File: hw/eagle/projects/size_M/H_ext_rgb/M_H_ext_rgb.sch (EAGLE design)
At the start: 6 parts

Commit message: pcb M.1 -not finished
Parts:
- removed U$2: RGB_WW-FCE50TC-Q1, !stavebnice03:RGB_WW-FCE50TC-Q1
- added H.D1: RGB_WW-FCE50TC-Q1, hugo:RGB_WW-FCE50TC-Q1
- H.R1, H.R2, H.R3: value 330 -> 82
- renumbered JP2 to H.J2, JP3 to H.J3, R1 to H.R1, R2 to H.R2, R3 to H.R3
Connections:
- net GND: now also H.D1.4, H.D1.5, H.D1.6, H.J3.4; no longer H.J3.3, U$2.4, U$2.5, U$2.6
- net N$1: now also H.D1.1; no longer U$2.1
- net N$2: now also H.D1.3; no longer U$2.3
- net N$3: now also H.D1.2; no longer U$2.2
- net VDD: now also H.J3.3; no longer H.J3.4
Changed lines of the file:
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@@
 </classes>
 <parts>
-<part name="JP2" library="pinhead2" deviceset="PINHD-1X6" device="" package3d_urn="urn:adsk.eagle:package:22472/2"/>
-<part name="U$2" library="!stavebnice03" deviceset="RGB_WW-FCE50TC-Q1" device=""/>
-<part name="R1" library="resistor" deviceset="R-EU_" device="R0603" value="330"/>
-<part name="R2" library="resistor" deviceset="R-EU_" device="R0603" value="330"/>
-<part name="R3" library="resistor" deviceset="R-EU_" device="R0603" value="330"/>
-<part name="JP3" library="pinhead2" deviceset="PINHD-1X5" device="" package3d_urn="urn:adsk.eagle:package:22469/2"/>
+<part name="H.J2" library="pinhead2" deviceset="PINHD-1X6" device="" package3d_urn="urn:adsk.eagle:package:22472/2"/>
+<part name="H.D1" library="hugo" deviceset="RGB_WW-FCE50TC-Q1" device=""/>
+<part name="H.R1" library="resistor" deviceset="R-EU_" device="R0603" value="82"/>
+<part name="H.R2" library="resistor" deviceset="R-EU_" device="R0603" value="82"/>
+<part name="H.R3" library="resistor" deviceset="R-EU_" device="R0603" value="82"/>
+<part name="H.J3" library="pinhead2" deviceset="PINHD-1X5" device="" package3d_urn="urn:adsk.eagle:package:22469/2"/>
 </parts>
 <sheets>
@@
 </plain>
 <instances>
-<instance part="JP2" gate="A" x="-15.24" y="48.26" smashed="yes" rot="R180">
+<instance part="H.J2" gate="A" x="-15.24" y="48.26" smashed="yes" rot="R180">
 <attribute name="NAME" x="-8.89" y="37.465" size="1.778" layer="95" rot="R180"/>
 <attribute name="VALUE" x="-8.89" y="58.42" size="1.778" layer="96" rot="R180"/>
 </instance>
-<instance part="U$2" gate="G$1" x="17.78" y="60.96" smashed="yes" rot="R180">
+<instance part="H.D1" gate="G$1" x="17.78" y="60.96" smashed="yes" rot="R180">
 <attribute name="NAME" x="27.94" y="66.04" size="1.27" layer="94" rot="R270"/>
 </instance>
-<instance part="R1" gate="G$1" x="5.08" y="86.36" smashed="yes" rot="MR180">
+<instance part="H.R1" gate="G$1" x="5.08" y="86.36" smashed="yes" rot="MR180">
 <attribute name="NAME" x="1.27" y="84.8614" size="1.778" layer="95" rot="MR180"/>
 <attribute name="VALUE" x="1.27" y="89.662" size="1.778" layer="96" rot="MR180"/>
 </instance>
-<instance part="R2" gate="G$1" x="5.08" y="78.74" smashed="yes" rot="MR180">
+<instance part="H.R2" gate="G$1" x="5.08" y="78.74" smashed="yes" rot="MR180">
 <attribute name="NAME" x="1.27" y="77.2414" size="1.778" layer="95" rot="MR180"/>
 <attribute name="VALUE" x="1.27" y="82.042" size="1.778" layer="96" rot="MR180"/>
 </instance>
-<instance part="R3" gate="G$1" x="5.08" y="71.12" smashed="yes" rot="MR180">
+<instance part="H.R3" gate="G$1" x="5.08" y="71.12" smashed="yes" rot="MR180">
 <attribute name="NAME" x="1.27" y="69.6214" size="1.778" layer="95" rot="MR180"/>
 <attribute name="VALUE" x="1.27" y="74.422" size="1.778" layer="96" rot="MR180"/>
 </instance>
-<instance part="JP3" gate="A" x="38.1" y="45.72" smashed="yes">
+<instance part="H.J3" gate="A" x="38.1" y="45.72" smashed="yes">
 <attribute name="NAME" x="31.75" y="53.975" size="1.778" layer="95"/>
 <attribute name="VALUE" x="31.75" y="35.56" size="1.778" layer="96"/>
@@
 <segment>
 <wire x1="17.78" y1="78.74" x2="10.16" y2="78.74" width="0.1524" layer="91"/>
-<pinref part="R2" gate="G$1" pin="2"/>
-<pinref part="U$2" gate="G$1" pin="2"/>
+<pinref part="H.R2" gate="G$1" pin="2"/>
+<pinref part="H.D1" gate="G$1" pin="2"/>
 <wire x1="17.78" y1="78.74" x2="17.78" y2="71.12" width="0.1524" layer="91"/>
 </segment>
@@
 <wire x1="12.7" y1="45.72" x2="22.86" y2="45.72" width="0.1524" layer="91"/>
 <junction x="12.7" y="45.72"/>
-<pinref part="U$2" gate="G$1" pin="6"/>
+<pinref part="H.D1" gate="G$1" pin="6"/>
 <wire x1="12.7" y1="48.26" x2="12.7" y2="45.72" width="0.1524" layer="91"/>
 <junction x="12.7" y="45.72"/>
-<pinref part="U$2" gate="G$1" pin="5"/>
+<pinref part="H.D1" gate="G$1" pin="5"/>
 <wire x1="17.78" y1="48.26" x2="17.78" y2="45.72" width="0.1524" layer="91"/>
 <junction x="17.78" y="45.72"/>
-<pinref part="U$2" gate="G$1" pin="4"/>
+<pinref part="H.D1" gate="G$1" pin="4"/>
 <wire x1="22.86" y1="48.26" x2="22.86" y2="45.72" width="0.1524" layer="91"/>
 <junction x="22.86" y="45.72"/>
-<wire x1="35.56" y1="45.72" x2="22.86" y2="45.72" width="0.1524" layer="91"/>
 <junction x="22.86" y="45.72"/>
-<pinref part="JP3" gate="A" pin="3"/>
-<pinref part="JP2" gate="A" pin="6"/>
+<pinref part="H.J2" gate="A" pin="6"/>
 <wire x1="-12.7" y1="53.34" x2="7.62" y2="53.34" width="0.1524" layer="91"/>
 <wire x1="7.62" y1="53.34" x2="7.62" y2="45.72" width="0.1524" layer="91"/>
 <wire x1="7.62" y1="45.72" x2="12.7" y2="45.72" width="0.1524" layer="91"/>
+<pinref part="H.J3" gate="A" pin="4"/>
+<wire x1="35.56" y1="43.18" x2="22.86" y2="43.18" width="0.1524" layer="91"/>
+<wire x1="22.86" y1="43.18" x2="22.86" y2="45.72" width="0.1524" layer="91"/>
 </segment>
 </net>
 <net name="N$1" class="0">
 <segment>
-<pinref part="R1" gate="G$1" pin="2"/>
-<pinref part="U$2" gate="G$1" pin="1"/>
+<pinref part="H.R1" gate="G$1" pin="2"/>
+<pinref part="H.D1" gate="G$1" pin="1"/>
 <wire x1="10.16" y1="86.36" x2="22.86" y2="86.36" width="0.1524" layer="91"/>
 <wire x1="22.86" y1="86.36" x2="22.86" y2="71.12" width="0.1524" layer="91"/>
@@
 <net name="N$2" class="0">
 <segment>
-<pinref part="R3" gate="G$1" pin="2"/>
-<pinref part="U$2" gate="G$1" pin="3"/>
+<pinref part="H.R3" gate="G$1" pin="2"/>
+<pinref part="H.D1" gate="G$1" pin="3"/>
 <wire x1="10.16" y1="71.12" x2="12.7" y2="71.12" width="0.1524" layer="91"/>
 </segment>
@@
 <net name="N$4" class="0">
 <segment>
-<pinref part="R1" gate="G$1" pin="1"/>
+<pinref part="H.R1" gate="G$1" pin="1"/>
 <wire x1="0" y1="86.36" x2="-7.62" y2="86.36" width="0.1524" layer="91"/>
 <wire x1="-7.62" y1="86.36" x2="-7.62" y2="50.8" width="0.1524" layer="91"/>
-<pinref part="JP2" gate="A" pin="5"/>
+<pinref part="H.J2" gate="A" pin="5"/>
 <wire x1="-7.62" y1="50.8" x2="-12.7" y2="50.8" width="0.1524" layer="91"/>
 </segment>
@@
 <net name="N$5" class="0">
 <segment>
-<pinref part="JP2" gate="A" pin="4"/>
+<pinref part="H.J2" gate="A" pin="4"/>
 <wire x1="-12.7" y1="48.26" x2="-5.08" y2="48.26" width="0.1524" layer="91"/>
-<pinref part="R2" gate="G$1" pin="1"/>
+<pinref part="H.R2" gate="G$1" pin="1"/>
 <wire x1="-5.08" y1="48.26" x2="-5.08" y2="78.74" width="0.1524" layer="91"/>
 <wire x1="-5.08" y1="78.74" x2="0" y2="78.74" width="0.1524" layer="91"/>
@@
 <net name="N$6" class="0">
 <segment>
-<pinref part="R3" gate="G$1" pin="1"/>
+<pinref part="H.R3" gate="G$1" pin="1"/>
 <wire x1="0" y1="71.12" x2="-2.54" y2="71.12" width="0.1524" layer="91"/>
 <wire x1="-2.54" y1="71.12" x2="-2.54" y2="45.72" width="0.1524" layer="91"/>
-<pinref part="JP2" gate="A" pin="3"/>
+<pinref part="H.J2" gate="A" pin="3"/>
 <wire x1="-2.54" y1="45.72" x2="-12.7" y2="45.72" width="0.1524" layer="91"/>
 </segment>
@@
 <net name="VDD" class="0">
 <segment>
-<pinref part="JP3" gate="A" pin="4"/>
-<wire x1="35.56" y1="43.18" x2="27.94" y2="43.18" width="0.1524" layer="91"/>
+<pinref part="H.J3" gate="A" pin="3"/>
+<wire x1="27.94" y1="45.72" x2="35.56" y2="45.72" width="0.1524" layer="91"/>
 </segment>
 </net>

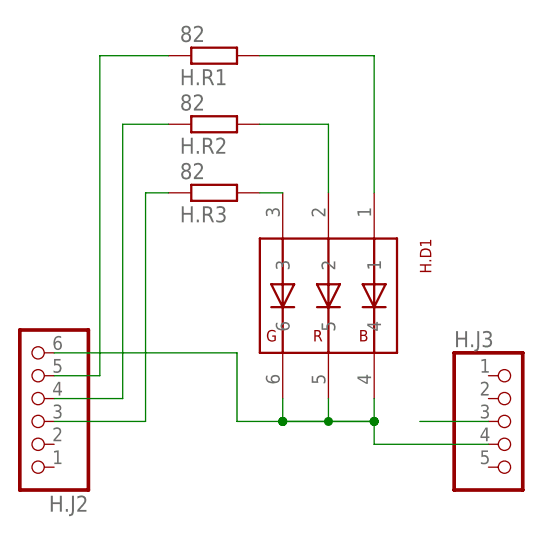
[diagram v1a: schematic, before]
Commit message: updateed PCBs - adjustments based on usage of version 1
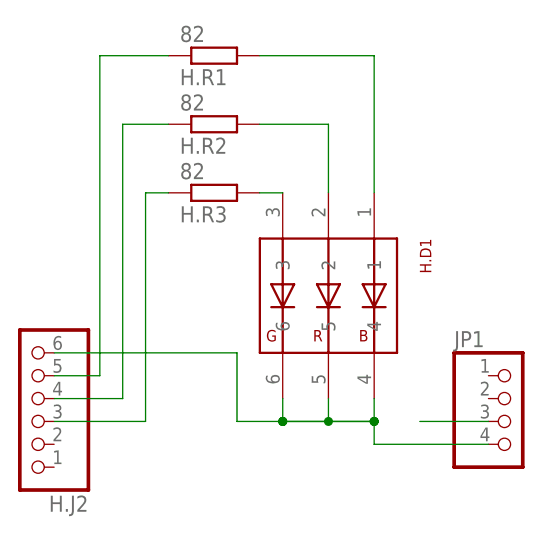
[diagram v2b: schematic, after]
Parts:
- removed H.J3: (no value), pinhead2:PINHD-1X5
- added JP1: (no value), pinhead2:PINHD-1X4
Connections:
- net GND: now also JP1.4; no longer H.J3.4
- net VDD: now also JP1.3; no longer H.J3.3
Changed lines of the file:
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@@
 <part name="H.R2" library="resistor" deviceset="R-EU_" device="R0603" value="82"/>
 <part name="H.R3" library="resistor" deviceset="R-EU_" device="R0603" value="82"/>
-<part name="H.J3" library="pinhead2" deviceset="PINHD-1X5" device="" package3d_urn="urn:adsk.eagle:package:22469/2"/>
+<part name="JP1" library="pinhead2" deviceset="PINHD-1X4" device="" package3d_urn="urn:adsk.eagle:package:22407/2"/>
 </parts>
 <sheets>
@@
 <attribute name="VALUE" x="1.27" y="74.422" size="1.778" layer="96" rot="MR180"/>
 </instance>
-<instance part="H.J3" gate="A" x="38.1" y="45.72" smashed="yes">
+<instance part="JP1" gate="A" x="38.1" y="45.72" smashed="yes">
 <attribute name="NAME" x="31.75" y="53.975" size="1.778" layer="95"/>
-<attribute name="VALUE" x="31.75" y="35.56" size="1.778" layer="96"/>
+<attribute name="VALUE" x="31.75" y="38.1" size="1.778" layer="96"/>
 </instance>
 </instances>
@@
 <wire x1="7.62" y1="53.34" x2="7.62" y2="45.72" width="0.1524" layer="91"/>
 <wire x1="7.62" y1="45.72" x2="12.7" y2="45.72" width="0.1524" layer="91"/>
-<pinref part="H.J3" gate="A" pin="4"/>
 <wire x1="35.56" y1="43.18" x2="22.86" y2="43.18" width="0.1524" layer="91"/>
 <wire x1="22.86" y1="43.18" x2="22.86" y2="45.72" width="0.1524" layer="91"/>
+<pinref part="JP1" gate="A" pin="4"/>
 </segment>
 </net>
@@
 <net name="VDD" class="0">
 <segment>
-<pinref part="H.J3" gate="A" pin="3"/>
-<wire x1="27.94" y1="45.72" x2="35.56" y2="45.72" width="0.1524" layer="91"/>
+<pinref part="JP1" gate="A" pin="3"/>
+<wire x1="35.56" y1="45.72" x2="27.94" y2="45.72" width="0.1524" layer="91"/>
 </segment>
 </net>
